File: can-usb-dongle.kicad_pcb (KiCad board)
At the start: 2 copper layers, 30 x 15 mm, 42 parts, among them SW1 SW_PUSH, U1 STM32F302C8T, U2 SN65HVD256, U3 NUF2042XV6, U4 MCP1700, U5 SiP32431, X1 16MHz 10ppm

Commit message: All components roughly placed.
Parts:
- R3, R4: moved to F.Cu
- moved C2 17.4 mm to (63.8, 51.5), turned to 180 degrees
- moved D2 13.8 mm to (68.8, 51.5), turned to 180 degrees
- moved D3 13.5 mm to (66.2, 51.5), turned to 0 degrees
- moved R7 12.2 mm to (64.8, 49.8)
- moved R6 12.1 mm to (68.0, 49.5)
- moved C9 11.2 mm to (66.0, 39.2), turned to 180 degrees
- moved C1 10.9 mm to (52.2, 50.4)
- moved C4 10.5 mm to (50.6, 50.8), turned to 90 degrees
- moved C3 8.36 mm to (64.5, 42.0)
- moved C14 7.96 mm to (67.0, 46.2), turned to 180 degrees
- moved R3 7.70 mm to (67.0, 39.2), turned to 90 degrees
- moved R1 7.60 mm to (55.2, 48.2), turned to 90 degrees
- moved R10 5.77 mm to (60.8, 39.0), turned to 270 degrees
- moved R4 5.66 mm to (65.5, 39.2)
- moved R9 5.44 mm to (65.2, 49.5), turned to 270 degrees
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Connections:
- net /V_BUS renamed /V_CAN_BUS
- U1 pad 2: /CAN1_STATUS_LED -> Net-(U1-Pad2)
- U1 pad 3: /CAN1_PWR_LED -> Net-(U1-Pad3)
- U1 pad 40: Net-(U1-Pad40) -> /CAN1_STATUS_LED
- U1 pad 41: Net-(U1-Pad41) -> /CAN1_PWR_LED
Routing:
- net Net-(C13-Pad1): track 4.63 -> 0.00 mm
- net Net-(CONN3-Pad3): track 2.50 -> 0.00 mm
- net Net-(CONN3-Pad2): track 2.44 -> 0.00 mm

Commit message: Start routing
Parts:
- R10, R11: moved to F.Cu
- R3, R4: moved to B.Cu
- moved C9 6.73 mm to (59.8, 41.8), turned to 270 degrees
- moved R10 5.51 mm to (66.2, 38.8), turned to 180 degrees
- moved R6 3.95 mm to (64.8, 51.8)
- moved C10 3.76 mm to (66.2, 48.0)
- moved C4 3.40 mm to (52.2, 47.8), turned to 180 degrees
- moved U5 2.74 mm to (67.7, 51.2), turned to 90 degrees
- moved R11 2.15 mm to (63.8, 38.8), turned to 180 degrees
- moved C14 1.95 mm to (68.2, 47.8), turned to 270 degrees
- moved R4 1.82 mm to (63.8, 38.8), turned to 180 degrees
- moved R8 1.13 mm to (52.2, 46.2), turned to 180 degrees
- moved C1 1.00 mm to (52.2, 49.4), turned to 180 degrees
- moved U3 0.97 mm to (52.2, 43.8)
- moved R3 0.90 mm to (66.2, 38.8), turned to 180 degrees
- moved U2 0.90 mm to (64.8, 44.2), turned to 0 degrees
- moved C3 0.85 mm to (64.8, 42.8), turned to 90 degrees
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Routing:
- net /BOOT0: track 0.00 -> 17.9 mm, vias 0 -> 1
- net /V_USB: track 0.00 -> 13.8 mm, vias 0 -> 1
- net /USB_D+: track 0.00 -> 13.8 mm, vias 0 -> 2
- net /V_CAN_BUS: track 0.00 -> 13.4 mm, vias 0 -> 1
- net Net-(CONN4-Pad4): track 0.00 -> 12.2 mm, vias 0 -> 2
- net /USB_D-: track 0.00 -> 12.1 mm
- net GND: track 0.00 -> 8.42 mm
- net /CAN1_TX: track 0.00 -> 8.18 mm, vias 0 -> 1
- net Net-(CONN4-Pad3): track 0.00 -> 8.02 mm, vias 0 -> 1
- net /SWDIO: track 0.00 -> 7.91 mm, vias 0 -> 1
- net /CAN_SILENT: track 0.00 -> 5.41 mm, vias 0 -> 1
- net /CAN1_RX: track 0.00 -> 5.20 mm, vias 0 -> 1
- net Net-(C13-Pad1): track 0.00 -> 4.76 mm
- net /SWCLK: track 0.00 -> 3.52 mm, vias 0 -> 1
- net Net-(D2-Pad2): track 0.00 -> 3.37 mm
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
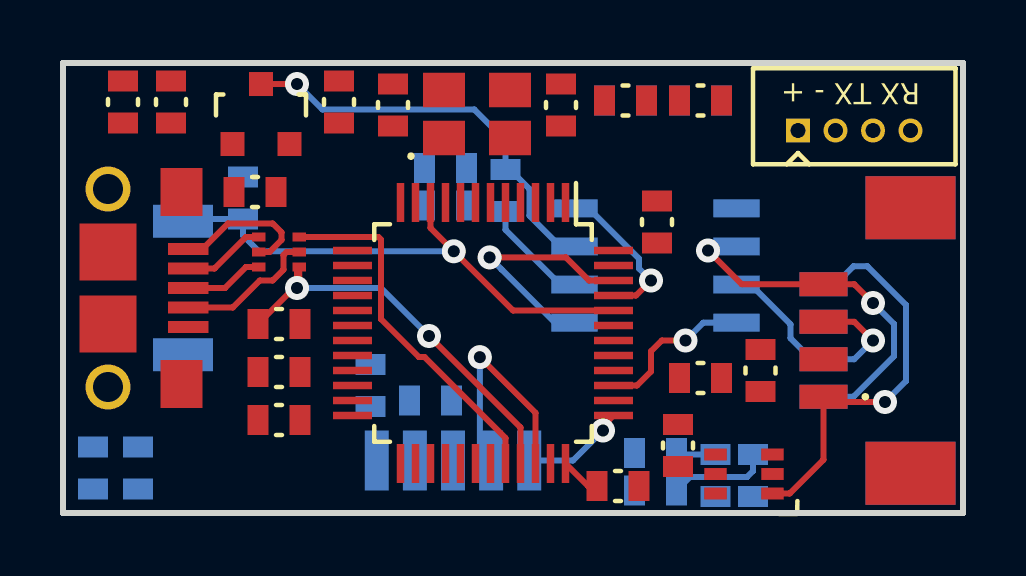
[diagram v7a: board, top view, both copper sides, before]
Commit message: Most traces fixed, need for optimization.
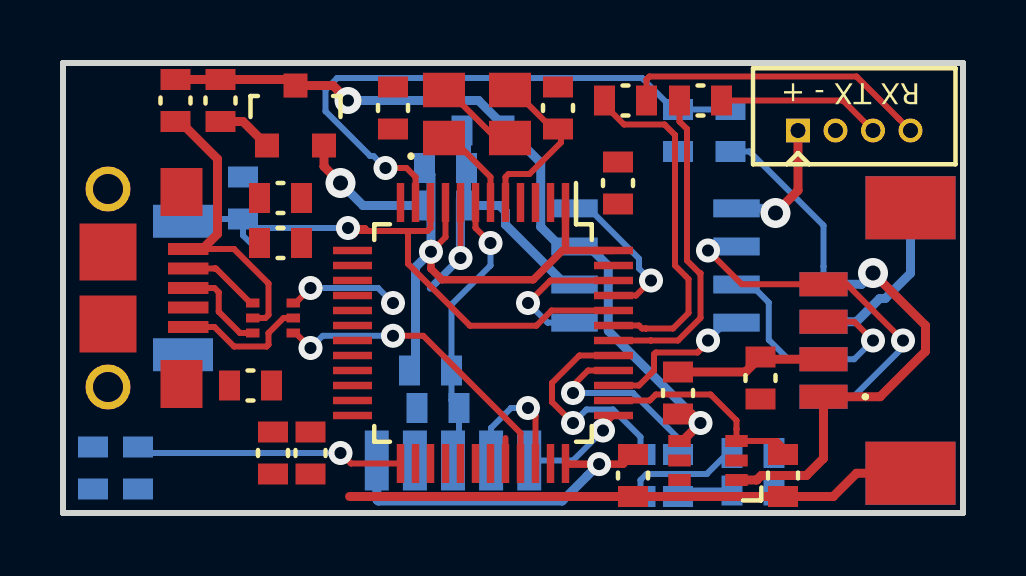
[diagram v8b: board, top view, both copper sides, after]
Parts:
- moved C12 3.75 mm to (52.2, 42.0), turned to 180 degrees
- moved R9 3.64 mm to (69.0, 51.2)
- moved C11 3.25 mm to (50.2, 38.8)
- moved C4 2.71 mm to (52.0, 50.5), turned to 270 degrees
- moved R10 2.50 mm to (63.8, 38.8)
- moved R11 2.50 mm to (66.2, 38.8)
- moved R8 2.26 mm to (51.2, 48.2), turned to 0 degrees
- moved U3 2.21 mm to (52.0, 46.0)
- moved C9 2.14 mm to (59.0, 39.8), turned to 180 degrees
- moved R1 2.06 mm to (57.2, 47.8), turned to 0 degrees
- moved R4 2.02 mm to (65.5, 39.8), turned to 270 degrees
- moved C13 1.90 mm to (52.2, 43.5)
- moved C3 1.84 mm to (63.5, 41.5)
- moved C1 1.52 mm to (53.2, 50.5), turned to 270 degrees
- moved D3 1.46 mm to (68.0, 50.5), turned to 180 degrees
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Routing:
- net GND: track 8.42 -> 52.0 mm, vias 0 -> 1
- net VCC: track 1.36 -> 38.8 mm, vias 0 -> 4
- net /V_BUS_SENSE: track 0.00 -> 19.6 mm, vias 0 -> 1
- net /V_USB: track 13.8 -> 26.7 mm, vias 1 -> 2
- net /UART1_RX: track 0.00 -> 11.8 mm
- net /UART1_TX: track 0.00 -> 10.8 mm
- net Net-(CONN1-Pad4): track 0.00 -> 10.3 mm
- net /NRST: track 0.00 -> 9.60 mm, vias 0 -> 1
- net /STATUS_LED: track 0.00 -> 8.98 mm, vias 0 -> 1
- net /V_CAN_BUS: track 13.4 -> 22.1 mm
- net /CAN1_PWR_LED: track 0.00 -> 7.46 mm, vias 0 -> 1
- net /USB_D-: track 12.1 -> 4.62 mm, vias 0 -> 2
- net /V_BUS_ENABLE: track 0.00 -> 6.86 mm
- net /CAN1_STATUS_LED: track 0.00 -> 6.48 mm, vias 0 -> 1
- net Net-(C8-Pad2): track 0.00 -> 5.92 mm
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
